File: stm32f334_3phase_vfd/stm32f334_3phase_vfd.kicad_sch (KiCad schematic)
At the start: 12 parts, among them J1 HV, J10 MH, J11 MH, J12 Conn_01x06, J2 PHA, J3 PHB, J4 PHC, J5 POWER_GND, J6 MH, J7 MH, J8 MH, J9 MH

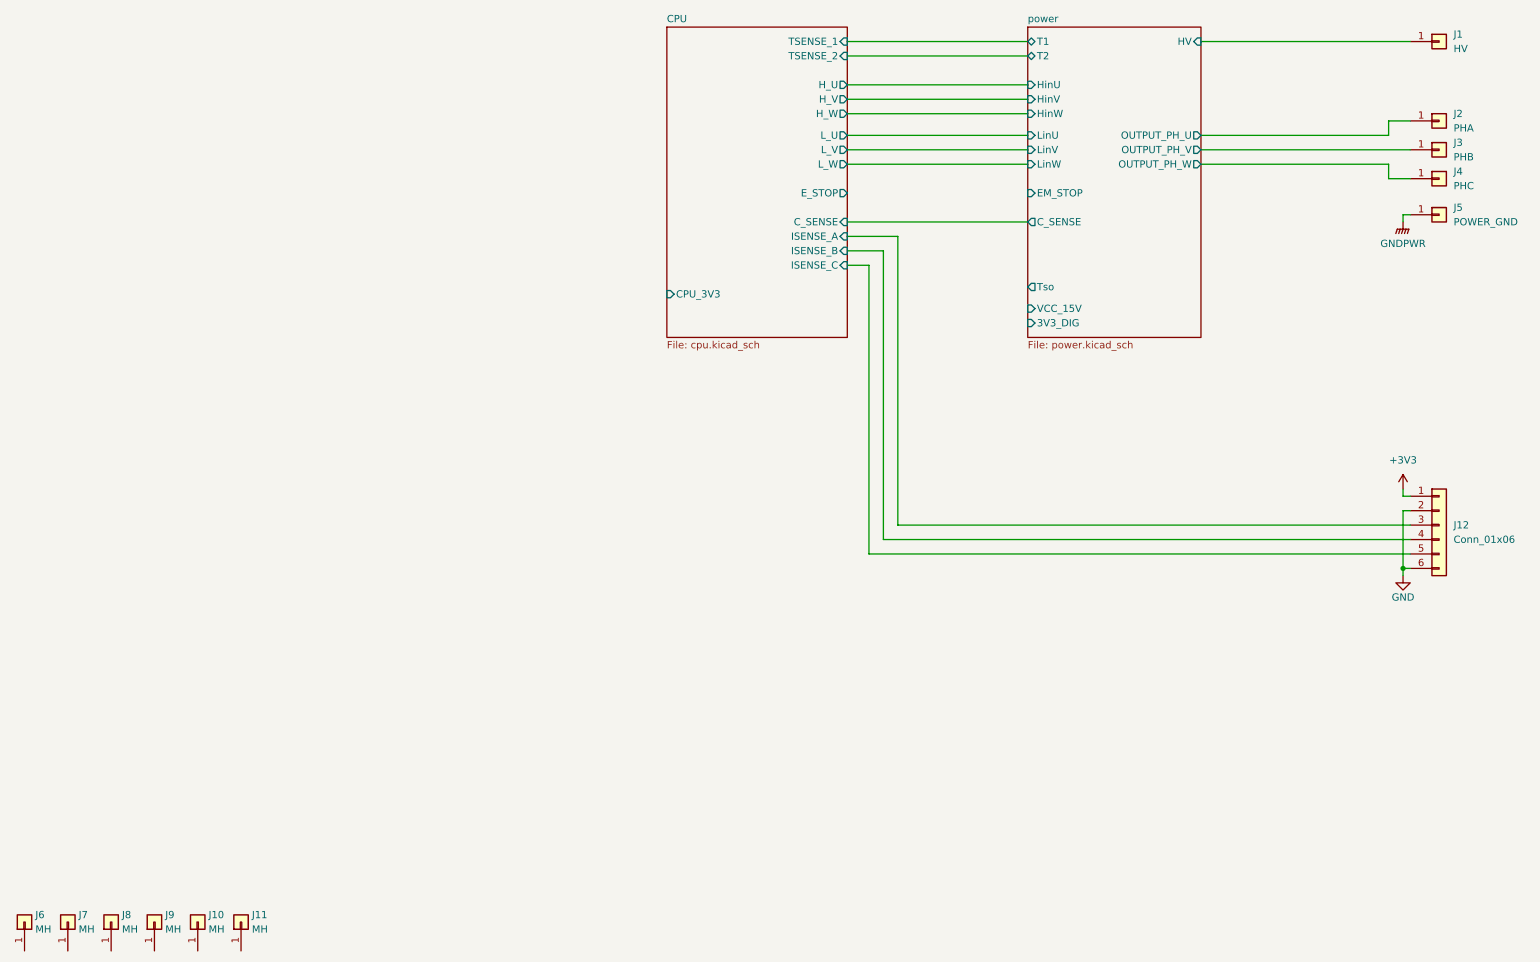
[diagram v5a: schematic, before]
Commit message: pcb fix and schematic clean-up
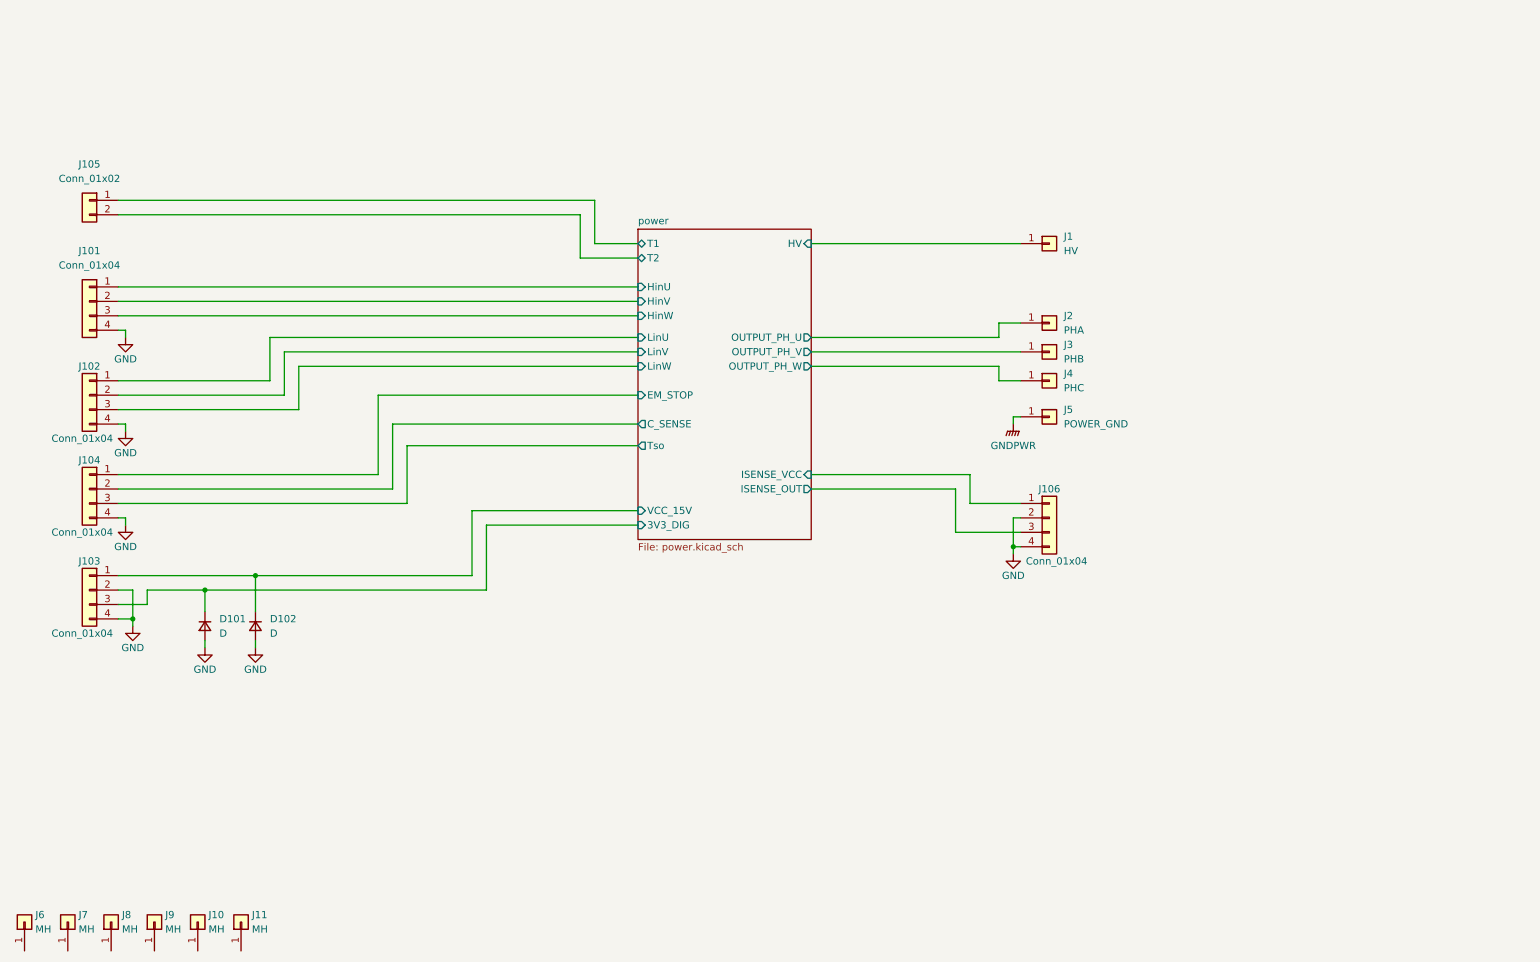
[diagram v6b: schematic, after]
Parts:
- removed J12: Conn_01x06, Connector_JST:JST_PH_B6B-PH-K_1x06_P2.00mm_Vertical, symbol Connector_Generic:Conn_01x06
- added D101, D102: D, Diode_SMD:D_SMA, symbol Device:D_Small
- added J101, J102, J103, J104, J106: Conn_01x04, Connector_JST:JST_PH_B4B-PH-K_1x04_P2.00mm_Vertical, symbol Connector_Generic:Conn_01x04
- added J105: Conn_01x02, Connector_JST:JST_PH_B2B-PH-K_1x02_P2.00mm_Vertical, symbol Connector_Generic:Conn_01x02
- J1, J2, J3, J4, J5: footprint stm32f334_3phase_vfd:1904969 -> stm32f334_3phase_vfd:KEYSTONE_7788
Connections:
- net GND: now also D101.2 (A), D102.2 (A), J101.4 (Pin_4), J102.4 (Pin_4), J103.2 (Pin_2), J103.4 (Pin_4), J104.4 (Pin_4), J106.2 (Pin_2), J106.4 (Pin_4)
- net power/3V3_DIG: now also D101.1 (K), J103.3 (Pin_3)
- net power/EM_STOP: now also J104.1 (Pin_1)
- net power/Tso: now also J104.3 (Pin_3)
- net power/VCC_15V: now also D102.1 (K), J103.1 (Pin_1)
- new net power/C_SENSE: J104.2 (Pin_2)
- new net power/HinU: J101.1 (Pin_1)
- new net power/HinV: J101.2 (Pin_2)
- new net power/HinW: J101.3 (Pin_3)
- new net power/ISENSE_OUT: J106.3 (Pin_3)
- new net power/ISENSE_VCC: J106.1 (Pin_1)
- new net power/LinU: J102.1 (Pin_1)
- new net power/LinV: J102.2 (Pin_2)
- new net power/LinW: J102.3 (Pin_3)
- new net power/T1: J105.1 (Pin_1)
- new net power/T2: J105.2 (Pin_2)
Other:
- removed sheet CPU
- sheet power ports: added ISENSE_OUT, ISENSE_VCC; removed none
- moved on the sheet: J1, J2, J3, J4, J5

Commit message: update schematic
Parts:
- removed J106: Conn_01x04, Connector_JST:JST_PH_B4B-PH-K_1x04_P2.00mm_Vertical, symbol Connector_Generic:Conn_01x04
- removed J11: MH, MountingHole:MountingHole_3.2mm_M3_Pad_TopBottom, symbol Connector_Generic:Conn_01x01
- added J106: Conn_01x06, Connector_JST:JST_PH_B6B-PH-K_1x06_P2.00mm_Vertical, symbol Connector_Generic:Conn_01x06
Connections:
- net GND: now also J106.2 (Pin_2), J106.6 (Pin_6)
- net power/ISENSE_VCC: now also J106.1 (Pin_1)
- new net power/IS_U: J106.3 (Pin_3)
- new net power/IS_V: J106.4 (Pin_4)
- new net power/IS_W: J106.5 (Pin_5)
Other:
- sheet power ports: added IS_U, IS_V, IS_W; removed ISENSE_OUT
